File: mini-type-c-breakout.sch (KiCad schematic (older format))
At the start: 11 parts, among them J0 TYPE-C-31-M12_13_EDITED, J1 ConnectionPoint, J2 ConnectionPoint, J3 ConnectionPoint, J4 ConnectionPoint, J5 ConnectionPoint, J6 ConnectionPoint, J7 ConnectionPoint, J8 ConnectionPoint

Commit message: v1.0a complete
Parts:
- removed J1, J2, J3, J4, J5, J6, J7, J8: ConnectionPoint, TestPoint:TestPoint_THTPad_1.0x1.0mm_Drill0.5mm, symbol mini_random_library:ConnectionPoint
- added J1, J2, J3, J6: Conn_01x01, TestPoint:TestPoint_Pad_1.0x1.0mm, symbol Connector_Generic:Conn_01x01
- J0: footprint mini-general-tweaks:TYPE-C-31-M-12-No-SHIELD -> mini-general-tweaks:HRO-TYPE-C-No-SHIELD
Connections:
- net GND: now also J6.1 (Pin_1)
- net USB_D+: now also J3.1 (Pin_1)
- net USB_D-: now also J2.1 (Pin_1)
- net VCC: now also J1.1 (Pin_1)
- net CC1: no longer names the net of J0.4 (CC1), R0.2
- net CC2: no longer names the net of J0.10 (CC2), R1.2
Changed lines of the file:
@@
 EESchema Schematic File Version 4
+LIBS:mini-type-c-breakout-cache
 EELAYER 30 0
 EELAYER END
@@
 Wire Wire Line
 	1600 950  1600 850
-Connection ~ 1600 850
 $Comp
 L power:VCC #PWR0103
@@
 Text GLabel 1650 2300 2    50   Input ~ 0
 USB_D+
-Connection ~ 1600 2100
-Connection ~ 1600 2300
-$Comp
-L mini_random_library:TYPE-C-31-M12_13_EDITED J0
-U 1 1 612F9EA6
-P 1000 2000
-F 0 "J0" H 1107 3417 50  0000 C CNN
-F 1 "TYPE-C-31-M12_13_EDITED" H 1107 3326 50  0000 C CNN
-F 2 "mini-general-tweaks:TYPE-C-31-M-12-No-SHIELD" V 500 2050 50  0001 C CNN
-F 3 "" H 1200 2050 50  0001 C CNN
-	1    1000 2000
-	1    0    0    -1
-$EndComp
 NoConn ~ 1600 3050
 NoConn ~ 1600 3150
-Wire Wire Line
-	900  3450 1000 3450
-Connection ~ 1000 3450
-Wire Wire Line
-	1000 3450 1100 3450
 $Comp
 L power:GND #PWR0104
@@
 	1    0    0    -1
 $EndComp
-$Comp
-L mini_random_library:ConnectionPoint J2
-U 1 1 61307277
-P 2950 1050
-F 0 "J2" H 3165 1097 50  0000 L CNN
-F 1 "ConnectionPoint" H 3165 1019 50  0000 L CNN
-F 2 "TestPoint:TestPoint_THTPad_1.0x1.0mm_Drill0.5mm" H 2950 950 50  0001 C CNN
-F 3 "" H 2950 950 50  0001 C CNN
-	1    2950 1050
-	1    0    0    -1
-$EndComp
-$Comp
-L mini_random_library:ConnectionPoint J3
-U 1 1 6130DB4A
-P 2950 1250
-F 0 "J3" H 3178 1301 50  0000 L CNN
-F 1 "ConnectionPoint" H 3178 1210 50  0000 L CNN
-F 2 "TestPoint:TestPoint_THTPad_1.0x1.0mm_Drill0.5mm" H 3250 1350 50  0001 C CNN
-F 3 "" H 3250 1350 50  0001 C CNN
-	1    2950 1250
-	1    0    0    -1
-$EndComp
-$Comp
-L mini_random_library:ConnectionPoint J6
-U 1 1 6130E898
-P 2950 1850
-F 0 "J6" H 3178 1901 50  0000 L CNN
-F 1 "ConnectionPoint" H 3178 1810 50  0000 L CNN
-F 2 "TestPoint:TestPoint_THTPad_1.0x1.0mm_Drill0.5mm" H 3250 1950 50  0001 C CNN
-F 3 "" H 3250 1950 50  0001 C CNN
-	1    2950 1850
-	1    0    0    -1
-$EndComp
-$Comp
-L mini_random_library:ConnectionPoint J1
-U 1 1 6130F2E8
-P 2950 850
-F 0 "J1" H 3178 901 50  0000 L CNN
-F 1 "ConnectionPoint" H 3178 810 50  0000 L CNN
-F 2 "TestPoint:TestPoint_THTPad_1.0x1.0mm_Drill0.5mm" H 3250 950 50  0001 C CNN
-F 3 "" H 3250 950 50  0001 C CNN
-	1    2950 850
-	1    0    0    -1
-$EndComp
-Text GLabel 1650 1550 3    50   Input ~ 0
-CC2
-Text GLabel 1650 1350 1    50   Input ~ 0
-CC1
 Wire Wire Line
 	1600 1550 1700 1550
 Wire Wire Line
 	1600 1350 1850 1350
-Text GLabel 2850 1450 0    50   Input ~ 0
-CC1
-Text GLabel 2850 1650 0    50   Input ~ 0
-CC2
-$Comp
-L mini_random_library:ConnectionPoint J4
-U 1 1 613173C0
-P 2950 1450
-F 0 "J4" H 3178 1501 50  0000 L CNN
-F 1 "ConnectionPoint" H 3178 1410 50  0000 L CNN
-F 2 "TestPoint:TestPoint_THTPad_1.0x1.0mm_Drill0.5mm" H 3250 1550 50  0001 C CNN
-F 3 "" H 3250 1550 50  0001 C CNN
-	1    2950 1450
-	1    0    0    -1
-$EndComp
-$Comp
-L mini_random_library:ConnectionPoint J5
-U 1 1 61318099
-P 2950 1650
-F 0 "J5" H 3178 1701 50  0000 L CNN
-F 1 "ConnectionPoint" H 3178 1610 50  0000 L CNN
-F 2 "TestPoint:TestPoint_THTPad_1.0x1.0mm_Drill0.5mm" H 3250 1750 50  0001 C CNN
-F 3 "" H 3250 1750 50  0001 C CNN
-	1    2950 1650
-	1    0    0    -1
-$EndComp
 Wire Wire Line
 	2850 850  2950 850
@@
 	2850 1250 2950 1250
 Wire Wire Line
-	2850 1450 2950 1450
-Wire Wire Line
-	2850 1650 2950 1650
-Wire Wire Line
 	2850 1850 2950 1850
 $Comp
-L power:GND #PWR0107
-U 1 1 61323410
-P 2850 2100
-F 0 "#PWR0107" H 2850 1850 50  0001 C CNN
-F 1 "GND" H 2855 1927 50  0000 C CNN
-F 2 "" H 2850 2100 50  0001 C CNN
-F 3 "" H 2850 2100 50  0001 C CNN
-	1    2850 2100
-	1    0    0    -1
-$EndComp
-$Comp
-L mini_random_library:ConnectionPoint J7
-U 1 1 61323416
-P 2950 2100
-F 0 "J7" H 3178 2151 50  0000 L CNN
-F 1 "ConnectionPoint" H 3178 2060 50  0000 L CNN
-F 2 "TestPoint:TestPoint_THTPad_1.0x1.0mm_Drill0.5mm" H 3250 2200 50  0001 C CNN
-F 3 "" H 3250 2200 50  0001 C CNN
-	1    2950 2100
-	1    0    0    -1
-$EndComp
-Wire Wire Line
-	2850 2100 2950 2100
-$Comp
-L power:GND #PWR0108
-U 1 1 613250BD
-P 2850 2350
-F 0 "#PWR0108" H 2850 2100 50  0001 C CNN
-F 1 "GND" H 2855 2177 50  0000 C CNN
-F 2 "" H 2850 2350 50  0001 C CNN
-F 3 "" H 2850 2350 50  0001 C CNN
-	1    2850 2350
-	1    0    0    -1
-$EndComp
-$Comp
-L mini_random_library:ConnectionPoint J8
-U 1 1 613250C3
-P 2950 2350
-F 0 "J8" H 3178 2401 50  0000 L CNN
-F 1 "ConnectionPoint" H 3178 2310 50  0000 L CNN
-F 2 "TestPoint:TestPoint_THTPad_1.0x1.0mm_Drill0.5mm" H 3250 2450 50  0001 C CNN
-F 3 "" H 3250 2450 50  0001 C CNN
-	1    2950 2350
-	1    0    0    -1
-$EndComp
-Wire Wire Line
-	2850 2350 2950 2350
+L Connector_Generic:Conn_01x01 J1
+U 1 1 612FE259
+P 3150 850
+F 0 "J1" H 3230 892 50  0000 L CNN
+F 1 "Conn_01x01" H 3230 801 50  0000 L CNN
+F 2 "TestPoint:TestPoint_Pad_1.0x1.0mm" H 3150 850 50  0001 C CNN
+F 3 "~" H 3150 850 50  0001 C CNN
+	1    3150 850
+	1    0    0    -1
+$EndComp
+$Comp
+L Connector_Generic:Conn_01x01 J2
+U 1 1 612FF83B
+P 3150 1050
+F 0 "J2" H 3230 1092 50  0000 L CNN
+F 1 "Conn_01x01" H 3230 1001 50  0000 L CNN
+F 2 "TestPoint:TestPoint_Pad_1.0x1.0mm" H 3150 1050 50  0001 C CNN
+F 3 "~" H 3150 1050 50  0001 C CNN
+	1    3150 1050
+	1    0    0    -1
+$EndComp
+$Comp
+L Connector_Generic:Conn_01x01 J3
+U 1 1 6130277F
+P 3150 1250
+F 0 "J3" H 3230 1292 50  0000 L CNN
+F 1 "Conn_01x01" H 3230 1201 50  0000 L CNN
+F 2 "TestPoint:TestPoint_Pad_1.0x1.0mm" H 3150 1250 50  0001 C CNN
+F 3 "~" H 3150 1250 50  0001 C CNN
+	1    3150 1250
+	1    0    0    -1
+$EndComp
+$Comp
+L Connector_Generic:Conn_01x01 J6
+U 1 1 61302F25
+P 3150 1850
+F 0 "J6" H 3230 1892 50  0000 L CNN
+F 1 "Conn_01x01" H 3230 1801 50  0000 L CNN
+F 2 "TestPoint:TestPoint_Pad_1.0x1.0mm" H 3150 1850 50  0001 C CNN
+F 3 "~" H 3150 1850 50  0001 C CNN
+	1    3150 1850
+	1    0    0    -1
+$EndComp
+Connection ~ 1600 2300
+Connection ~ 1600 2100
+Connection ~ 1600 850
+Wire Wire Line
+	1000 3450 1100 3450
+Wire Wire Line
+	900  3450 1000 3450
+Connection ~ 1000 3450
+$Comp
+L mini_random_library:TYPE-C-31-M12_13_EDITED J0
+U 1 1 612F9EA6
+P 1000 2000
+F 0 "J0" H 1107 3417 50  0000 C CNN
+F 1 "TYPE-C-31-M12_13_EDITED" H 1107 3326 50  0000 C CNN
+F 2 "mini-general-tweaks:HRO-TYPE-C-No-SHIELD" V 500 2050 50  0001 C CNN
+F 3 "" H 1200 2050 50  0001 C CNN
+	1    1000 2000
+	1    0    0    -1
+$EndComp
 $EndSCHEMATC

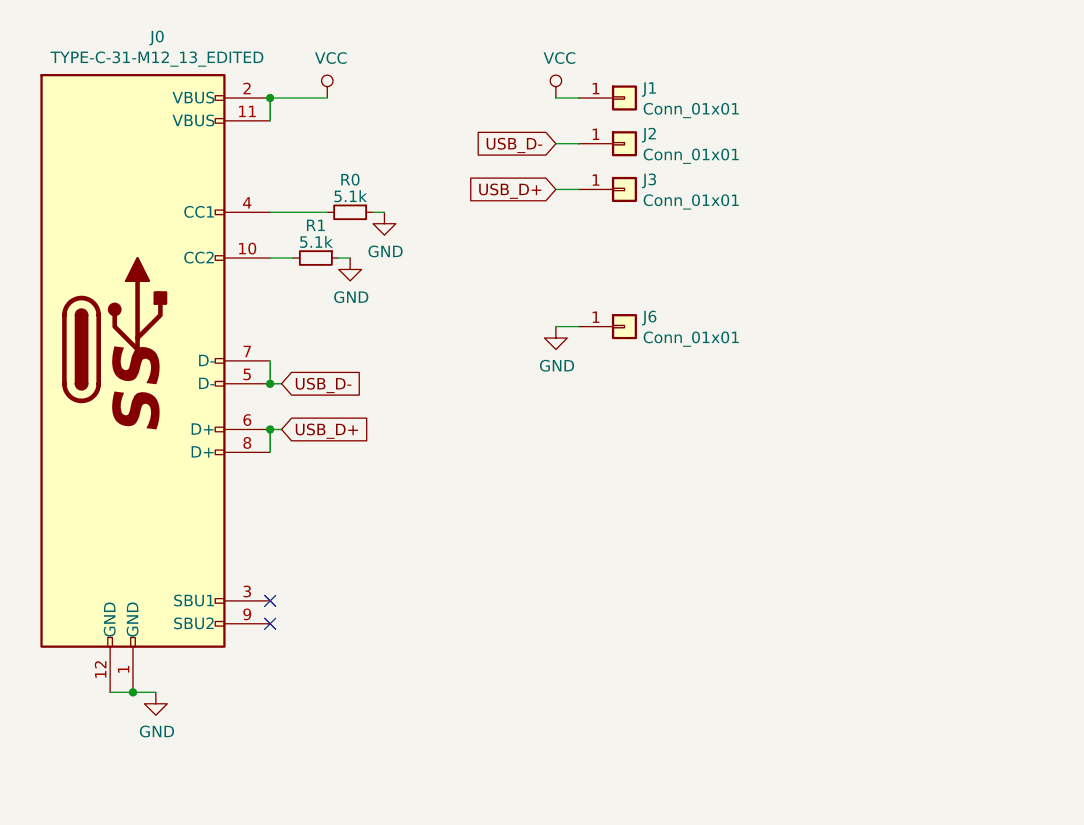
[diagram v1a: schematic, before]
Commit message: Many tweaks, additions, etc.
Added licensing, tweaked PCB silkscreen, added logos to schematic, tweaked schematic layout, etc.
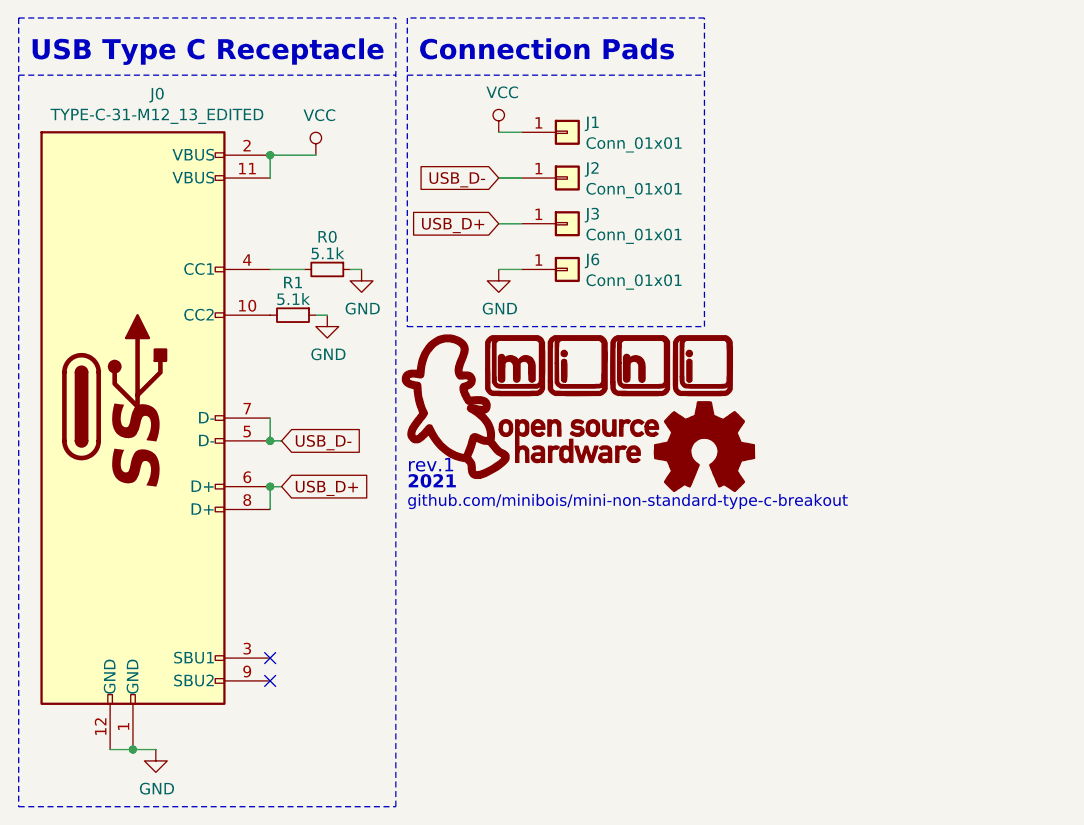
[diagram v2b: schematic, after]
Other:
- note added: "2021"
- note added: "Connection Pads"
- note added: "USB Type C Receptacle"
- note added: "github.com/minibois/mini-non-standard-type-c-breakout"
- note added: "rev.1"
- moved on the sheet: J0, J1, J2, J3, J6, R0, R1

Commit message: Updated URL in schematic
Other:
- note added: "https://github.com/minibois/non-standard-type-c-breakout/"
- note removed: "github.com/minibois/mini-non-standard-type-c-breakout"
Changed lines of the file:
@@
 encoding utf-8
 Sheet 1 1
-Title ""
-Date ""
-Rev ""
-Comp ""
-Comment1 ""
-Comment2 ""
-Comment3 ""
-Comment4 ""
+Title "non standard type c breakout board"
+Date "2021-10-18"
+Rev "1"
+Comp "github.com/minibois/non-standard-type-c-breakout/blob/master/LICENSE/LICENSE.txt"
+Comment1 "of CERN_OHL-S v2 (https://ohwr.org/cern_ohl_s_v2.txt)"
+Comment2 "You may redistribute and modify this source and make products using it under the terms"
+Comment3 "This schematic describes Open Hardware and is licensed under the CERN-OHL-S v2."
+Comment4 "Copyright minibois 2021. "
 $EndDescr
+Text Notes 2200 2650 0    50   ~ 0
+https://github.com/minibois/non-standard-type-c-breakout/
 Wire Wire Line
 	1600 2650 1600 2550
@@
 Text Notes 2200 2500 0    59   ~ 0
 rev.1
-Text Notes 2200 2650 0    50   ~ 0
-github.com/minibois/mini-non-standard-type-c-breakout
 $EndSCHEMATC
